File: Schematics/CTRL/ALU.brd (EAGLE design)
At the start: 135.9 x 135.6 mm, 42 parts

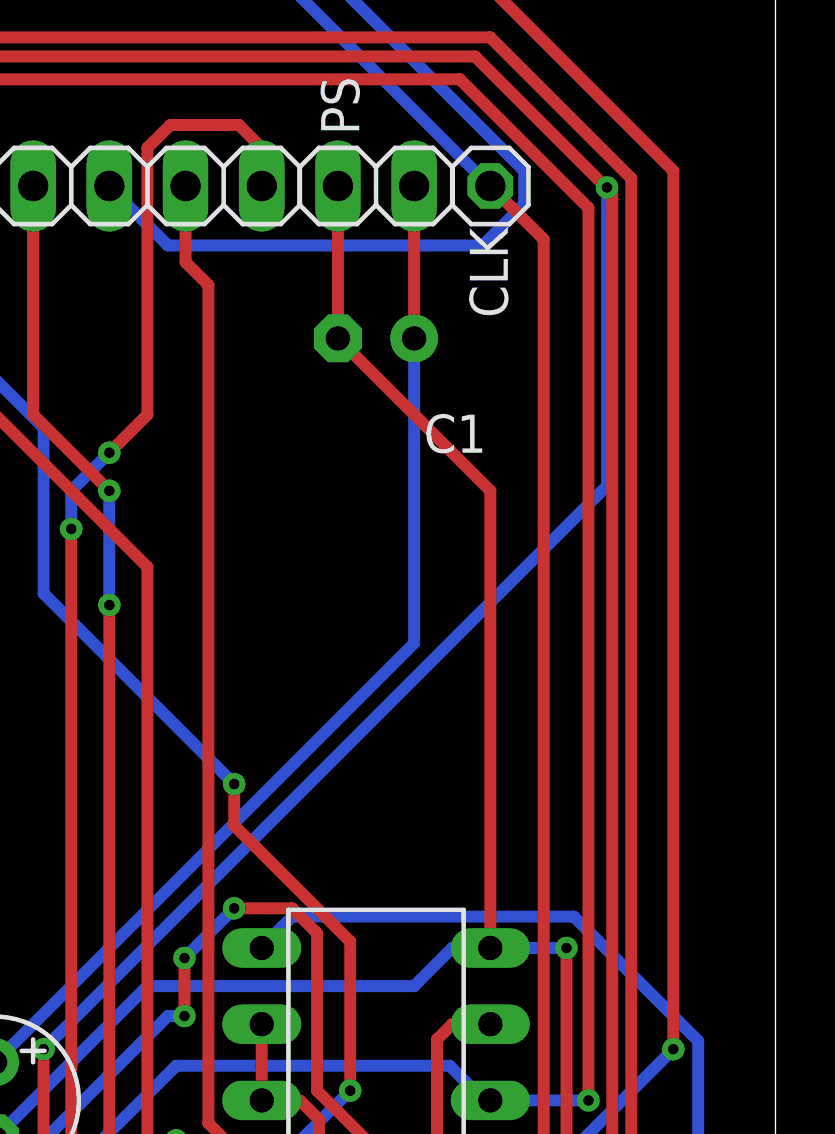
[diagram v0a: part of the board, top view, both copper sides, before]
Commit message: Added bus, fixed C1 on ALU-CTRL, CLK.zip, added 7410 to ctrl so bus out will work*.
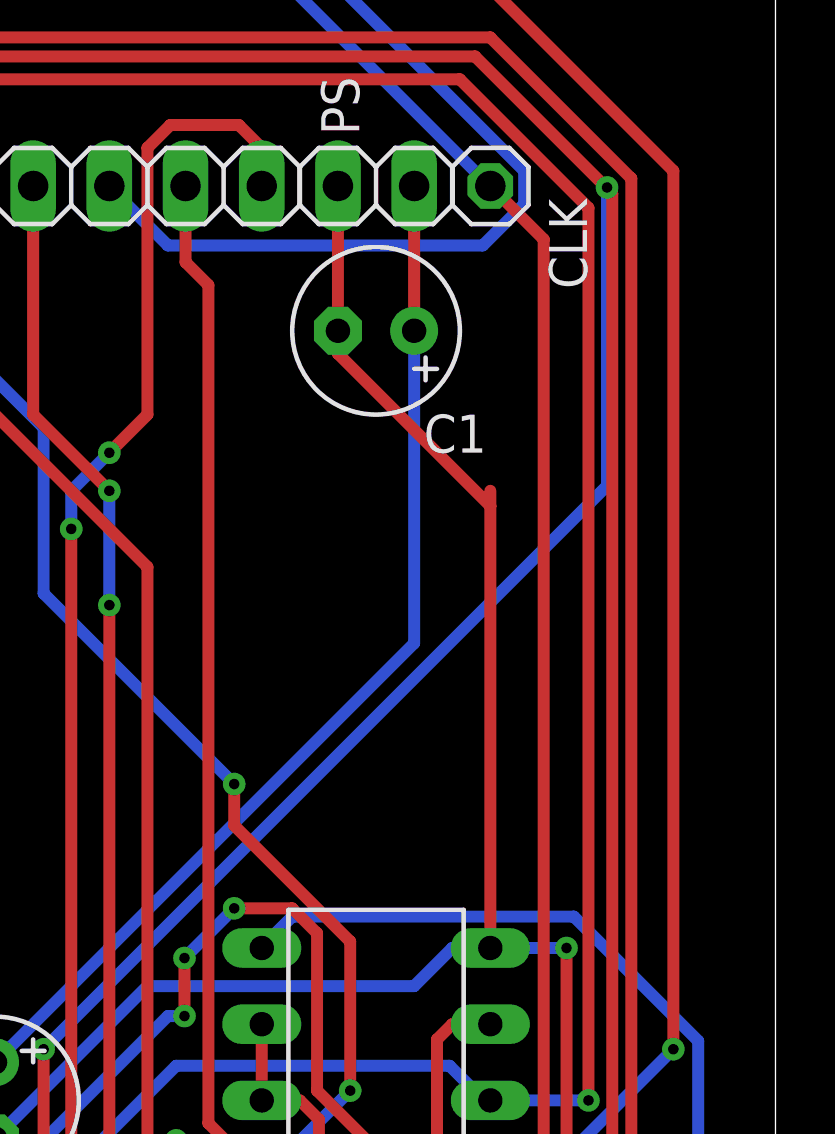
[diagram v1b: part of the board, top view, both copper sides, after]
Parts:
- moved C1 0.25 mm to (122.6, 113.8), flipped to the top, turned to 180 degrees
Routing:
- net GND: track 693.9 -> 694.4 mm
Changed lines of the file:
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@@
 <drawing>
 <settings>
-<setting alwaysvectorfont="yes"/>
+<setting alwaysvectorfont="no"/>
 <setting verticaltext="up"/>
 </settings>
@@
 <elements>
 <element name="CLK" library="pinhead" library_urn="urn:adsk.eagle:library:325" package="1X01" package3d_urn="urn:adsk.eagle:package:22485/2" value="" x="126.365" y="118.618" smashed="yes">
-<attribute name="NAME" x="126.9492" y="114.2238" size="1.27" layer="25" ratio="10" rot="R90"/>
+<attribute name="NAME" x="128.3208" y="118.1862" size="1.27" layer="25" ratio="10" rot="R270"/>
 <attribute name="POPULARITY" value="64" x="177.165" y="30.988" size="1.778" layer="27" display="off"/>
 <attribute name="VALUE" x="125.095" y="115.443" size="1.27" layer="27"/>
@@
 <attribute name="VALUE" x="38.354" y="101.473" size="1.27" layer="27" ratio="10"/>
 </element>
-<element name="C1" library="rcl" library_urn="urn:adsk.eagle:library:334" package="E2,5-6" package3d_urn="urn:adsk.eagle:package:23349/1" value="" x="122.555" y="113.538" smashed="yes" rot="MR0">
+<element name="C1" library="rcl" library_urn="urn:adsk.eagle:library:334" package="E2,5-6" package3d_urn="urn:adsk.eagle:package:23349/1" value="" x="122.555" y="113.792" smashed="yes" rot="R180">
 <attribute name="NAME" x="126.238" y="110.998" size="1.27" layer="25" ratio="10" rot="R180"/>
-<attribute name="POPULARITY" value="26" x="122.555" y="113.538" size="1.778" layer="28" rot="MR0" display="off"/>
-<attribute name="SPICEPREFIX" value="C" x="122.555" y="113.538" size="1.778" layer="28" rot="MR0" display="off"/>
-<attribute name="VALUE" x="119.888" y="110.871" size="1.27" layer="28" ratio="10" rot="MR0"/>
+<attribute name="POPULARITY" value="26" x="122.555" y="113.792" size="1.778" layer="27" rot="R180" display="off"/>
+<attribute name="SPICEPREFIX" value="C" x="122.555" y="113.792" size="1.778" layer="27" rot="R180" display="off"/>
+<attribute name="VALUE" x="119.888" y="116.459" size="1.27" layer="27" ratio="10" rot="R180"/>
 </element>
 <element name="C2" library="rcl" library_urn="urn:adsk.eagle:library:334" package="E2,5-6" package3d_urn="urn:adsk.eagle:package:23349/1" value="" x="59.055" y="29.718" smashed="yes" rot="R270">
@@
 <contactref element="C8" pad="+"/>
 <contactref element="C9" pad="+"/>
-<wire x1="123.825" y1="113.538" x2="123.825" y2="118.618" width="0.4" layer="1"/>
 <wire x1="126.365" y1="47.498" x2="126.365" y2="48.768" width="0.4" layer="1"/>
 <wire x1="126.365" y1="48.768" x2="123.825" y2="51.308" width="0.4" layer="1"/>
@@
 <wire x1="31.115" y1="11.938" x2="32.385" y2="13.208" width="0.4" layer="16"/>
 <wire x1="109.855" y1="89.408" x2="123.825" y2="103.378" width="0.4" layer="16"/>
-<wire x1="123.825" y1="103.378" x2="123.825" y2="113.538" width="0.4" layer="16"/>
 <wire x1="37.465" y1="33.528" x2="34.925" y2="33.528" width="0.4" layer="16"/>
 <wire x1="34.925" y1="33.528" x2="19.685" y2="33.528" width="0.4" layer="16"/>
@@
 <wire x1="89.378" y1="61.6722" x2="89.535" y2="61.468" width="0.4" layer="16"/>
 <wire x1="104.569" y1="70.2344" x2="104.775" y2="70.358" width="0.4" layer="16"/>
+<wire x1="123.825" y1="103.378" x2="123.825" y2="113.792" width="0.4" layer="16"/>
+<wire x1="123.825" y1="118.618" x2="123.825" y2="113.792" width="0.4" layer="1"/>
 </signal>
 <signal name="GND">
@@
 <contactref element="C4" pad="-"/>
 <contactref element="C3" pad="-"/>
-<wire x1="121.285" y1="118.618" x2="121.285" y2="113.538" width="0.4" layer="1"/>
-<wire x1="121.285" y1="113.538" x2="126.365" y2="108.458" width="0.4" layer="1"/>
-<wire x1="126.365" y1="108.458" x2="126.365" y2="93.218" width="0.4" layer="1"/>
+<wire x1="126.365" y1="108.458" x2="126.365" y2="107.95" width="0.4" layer="1"/>
+<wire x1="126.365" y1="107.95" x2="126.365" y2="93.218" width="0.4" layer="1"/>
 <wire x1="64.135" y1="47.498" x2="62.865" y2="48.768" width="0.4" layer="1"/>
 <wire x1="62.865" y1="60.198" x2="64.135" y2="61.468" width="0.4" layer="1"/>
@@
 <via x="95.4544" y="42.8906" extent="1-16" drill="0.35"/>
 <via x="115.8932" y="65.8152" extent="1-16" drill="0.35"/>
+<wire x1="126.365" y1="107.95" x2="121.285" y2="113.03" width="0.4" layer="1"/>
+<wire x1="121.285" y1="113.03" x2="121.285" y2="113.792" width="0.4" layer="1"/>
+<wire x1="121.285" y1="113.792" x2="121.285" y2="118.618" width="0.4" layer="1"/>
 </signal>
 <signal name="CLK">
